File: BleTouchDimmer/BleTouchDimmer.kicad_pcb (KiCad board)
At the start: 2 copper layers, 28 parts, among them P1 PROG, P2 UART, Q1 PDTC123J, SW1 SW_PUSH, U1 LTV-814, U2 MDBT40, U3 MOC3021S, Y2 Crystal

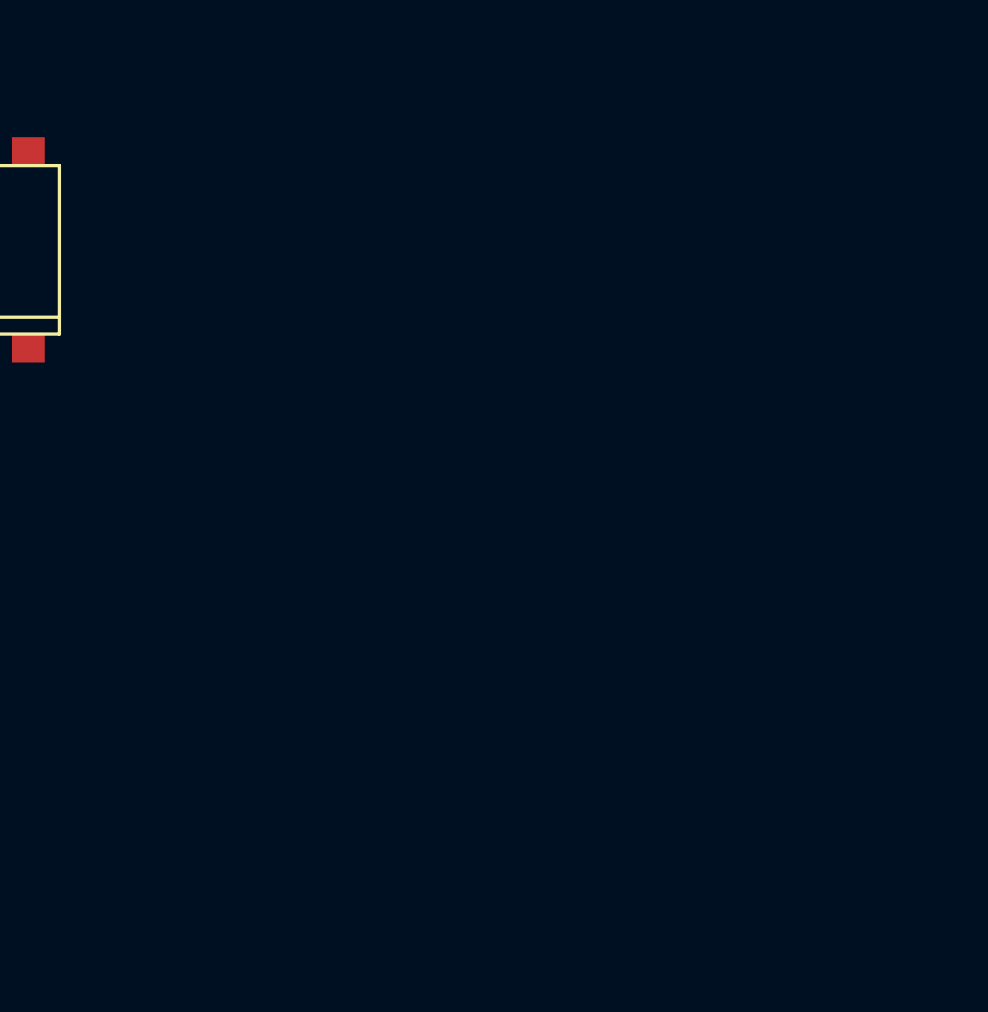
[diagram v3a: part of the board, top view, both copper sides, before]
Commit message: Added triacs.
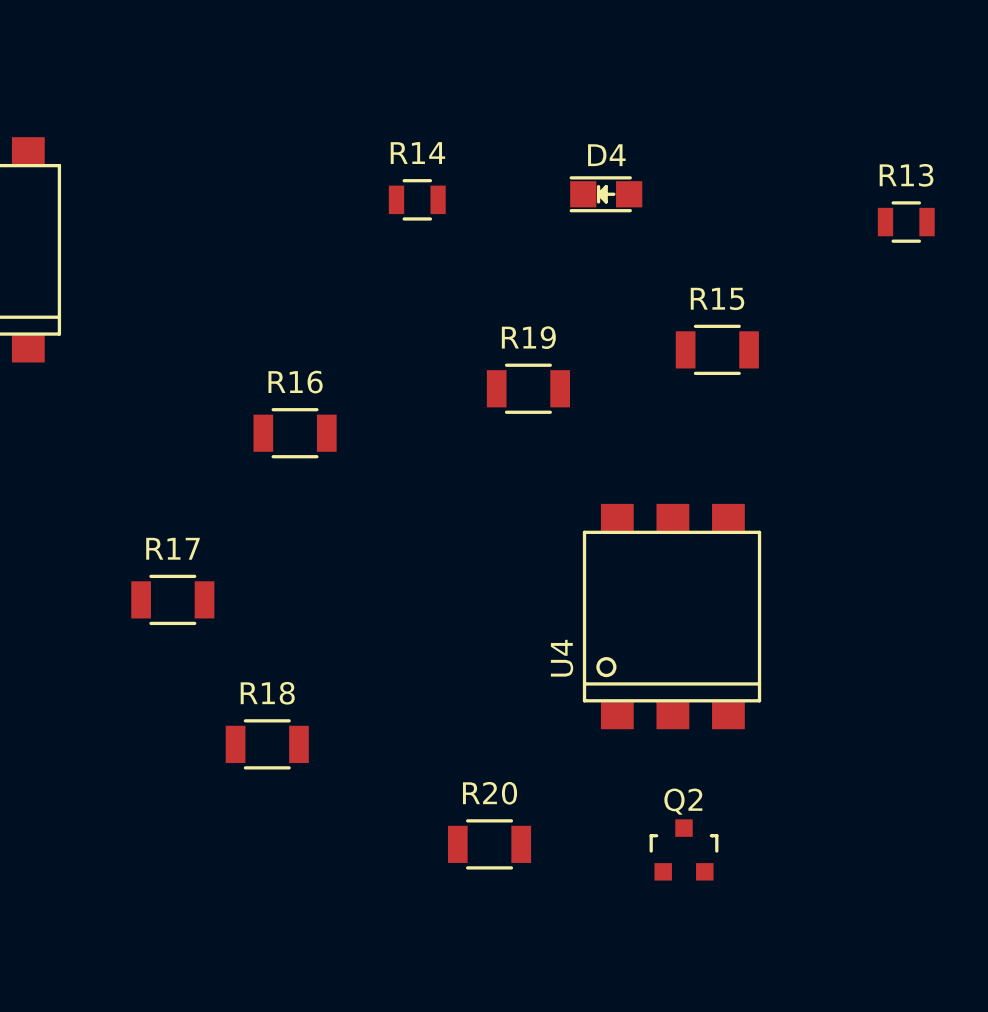
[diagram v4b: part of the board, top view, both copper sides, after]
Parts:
- added D4: LED, LEDs:LED_0805, F.Cu at (190.8, 68.6)
- added Q2: PDTC123J, TO_SOT_Packages_SMD:SOT-23, F.Cu at (194.3, 98.6)
- added R13: 100R, Resistors_SMD:R_0805, F.Cu at (204.5, 69.8)
- added R14: 220R, Resistors_SMD:R_0805, F.Cu at (182.1, 68.8)
- added R15: 360R, Resistors_SMD:R_1206, F.Cu at (195.8, 75.7)
- added R16: 360R, Resistors_SMD:R_1206, F.Cu at (176.5, 79.5)
- added R17: 360R, Resistors_SMD:R_1206, F.Cu at (170.9, 87.1)
- added R18: 360R, Resistors_SMD:R_1206, F.Cu at (175.3, 93.7)
- added R19: 360R, Resistors_SMD:R_1206, F.Cu at (187.2, 77.5)
- added R20: 360R, Resistors_SMD:R_1206, F.Cu at (185.4, 98.3)
- added U4: MOC3021S, EgertKiCad_lib:MOC3021S, F.Cu at (191.3, 87.9)
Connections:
- U3 pad 4: (no net) -> Net-(R16-Pad1)
- U3 pad 6: (no net) -> Net-(R15-Pad1)

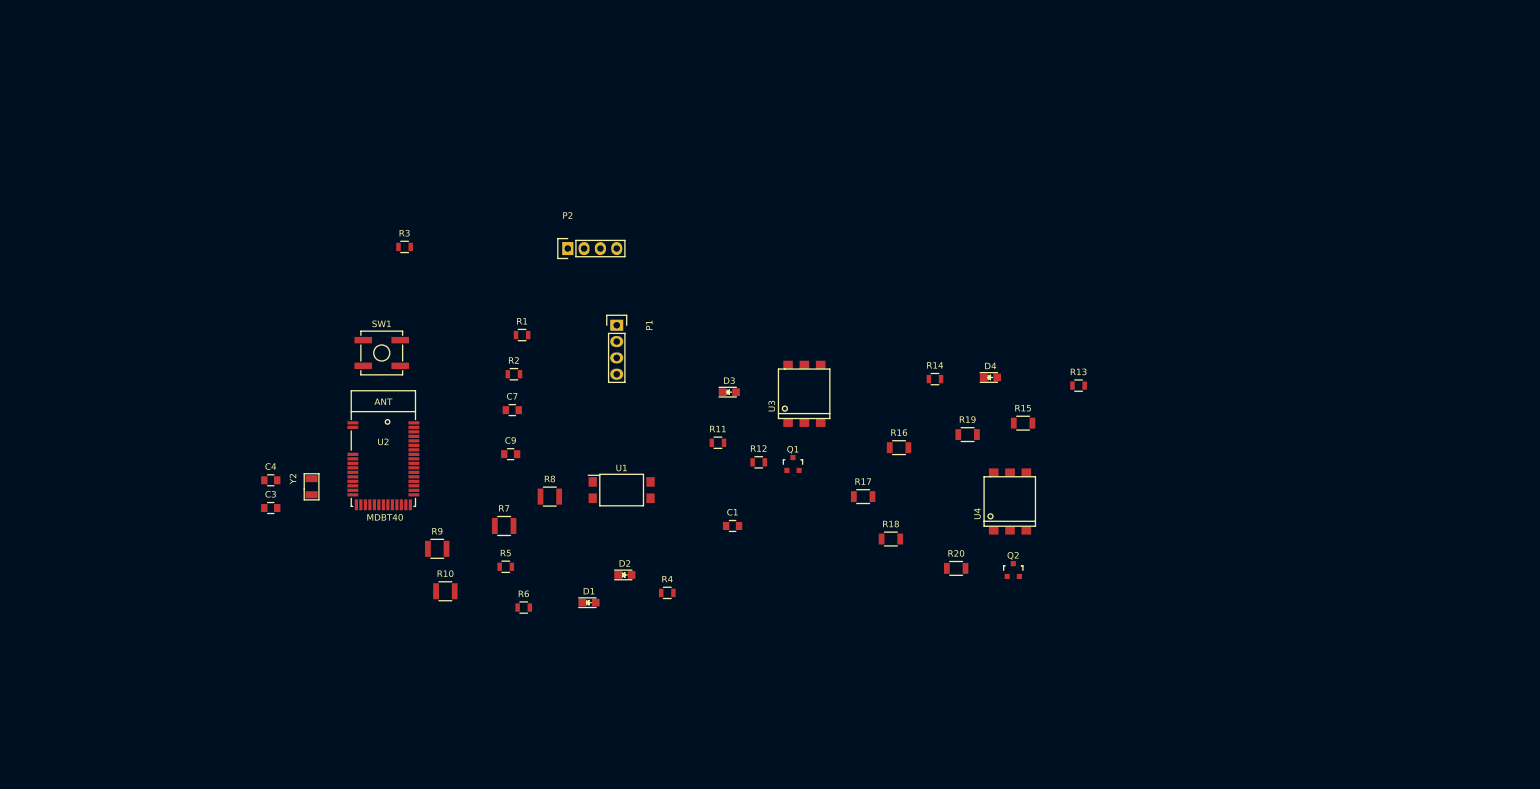
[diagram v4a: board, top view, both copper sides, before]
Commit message: Added isolation transformer:D
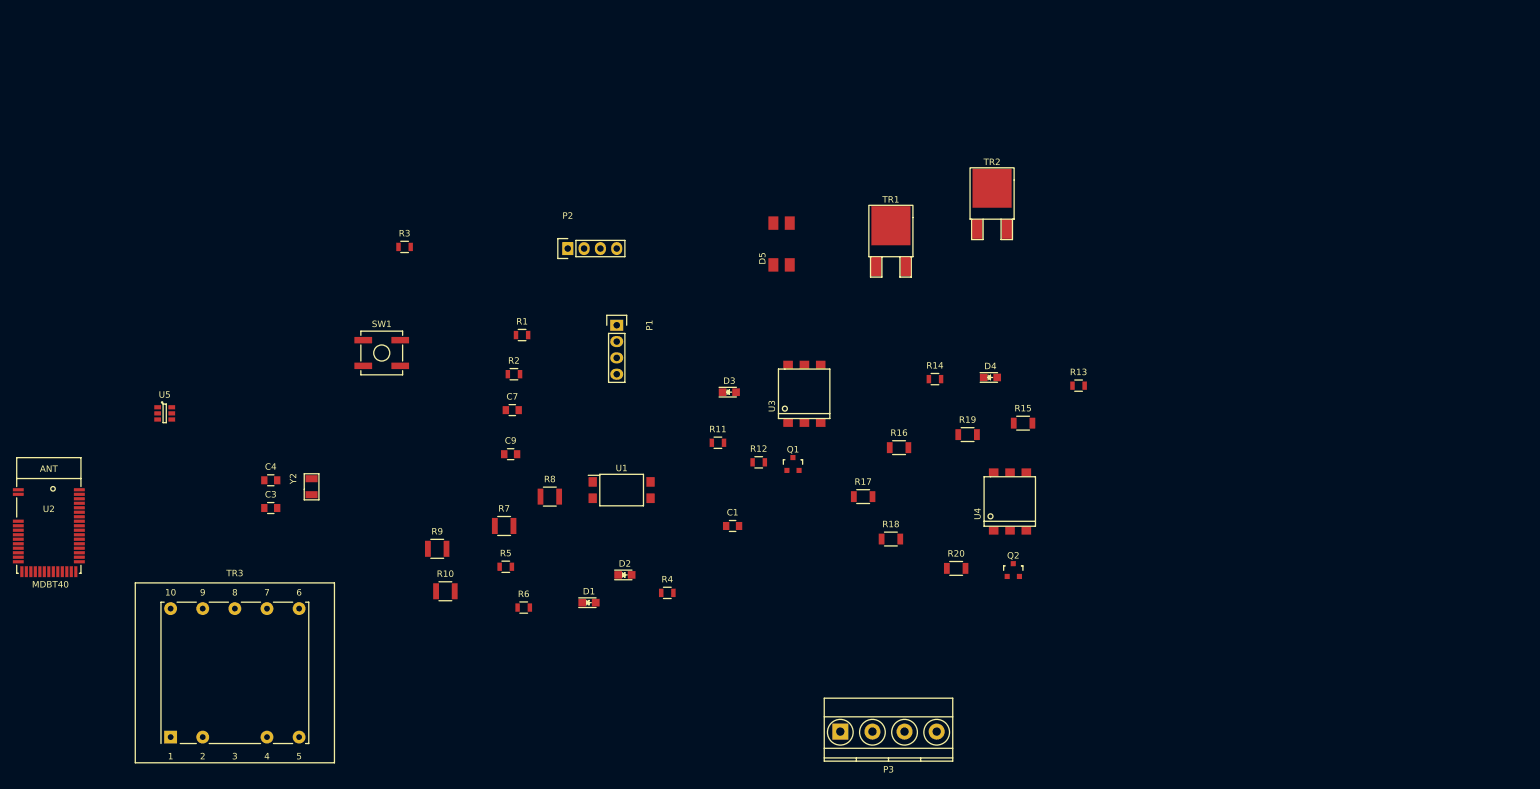
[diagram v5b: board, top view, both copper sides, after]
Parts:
- added D5: Diode_Bridge, EgertKiCad_lib:SOIC-4, F.Cu at (157.0, 51.1)
- added P3: POWER, Terminal_Blocks:TerminalBlock_Pheonix_MKDS1.5-4pol, F.Cu at (167.4, 123.7)
- added TR1: TRIAC, TO_SOT_Packages_SMD:TO-252-2Lead, F.Cu at (175.3, 51.3)
- added TR2: TRIAC, TO_SOT_Packages_SMD:TO-252-2Lead, F.Cu at (191.0, 45.5)
- added TR3: TEZ1.5-D-1, TEZ-28x33, F.Cu at (73.2, 114.6)
- added U5: LNK4002S, TO_SOT_Packages_SMD:SOT-23-6, F.Cu at (62.2, 74.2)
- moved U2 53.1 mm to (44.2, 99.1)
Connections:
- R19 pad 2: (no net) -> /TRIACS/TRIAC1_L_OUT
- R20 pad 2: (no net) -> /TRIACS/TRIAC2_L_OUT

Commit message: Updated schematic.
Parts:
- added C2: 100n, Capacitors_SMD:C_0603, F.Cu at (273.0, 36.6)
- added C6: 10uF, Capacitors_SMD:C_0603, F.Cu at (226.9, 68.4)
- added C8: 22uF, Capacitors_SMD:C_0603, F.Cu at (218.8, 73.0)
- added D6: Led_Small, LEDs:LED_0603, F.Cu at (220.7, 68.1)
- added J1: Conn_01x03, Connectors_Molex:Molex_SPOX-5267_22-03-5035_03x2.54mm_Straight, F.Cu at (237.5, 47.3)
- added J2: Conn_01x03, Connectors_Molex:Molex_SPOX-5267_22-03-5035_03x2.54mm_Straight, F.Cu at (255.5, 38.9)
- added J3: JTAG, Connectors_Molex:Molex_SPOX-5267_22-03-5075_07x2.54mm_Straight, F.Cu at (219.4, 38.9)
- added J4: Conn_01x06, Connectors_Molex:Molex_SPOX-5267_22-03-5065_06x2.54mm_Straight, F.Cu at (219.4, 47.3)
- added J5: SLIDER1, Connectors_Molex:Molex_SPOX-5267_22-03-5055_05x2.54mm_Straight, F.Cu at (240.0, 38.9)
- added J6: SLIDER2, Connectors_Molex:Molex_SPOX-5267_22-03-5055_05x2.54mm_Straight, F.Cu at (219.4, 55.7)
- added Q3: PDTC123J, TO_SOT_Packages_SMD:SOT-23, F.Cu at (249.2, 46.0)
- added Q4: PDTC123J, TO_SOT_Packages_SMD:SOT-23, F.Cu at (249.2, 53.0)
- added Q5: BC850, TO_SOT_Packages_SMD:SOT-23, F.Cu at (261.2, 46.0)
- added Q6: BC850, TO_SOT_Packages_SMD:SOT-23, F.Cu at (255.8, 46.0)
- added R21: 100R, Resistors_SMD:R_0603, F.Cu at (223.1, 73.4)
- added R23: 0R, Resistors_SMD:R_0603, F.Cu at (243.9, 59.0)
- added R24: 0R, Resistors_SMD:R_0603, F.Cu at (265.0, 36.5)
- added R25: 0R, Resistors_SMD:R_0603, F.Cu at (254.9, 52.0)
- added R26: 0R, Resistors_SMD:R_0603, F.Cu at (247.3, 59.0)
- added R27: 2k2, Resistors_SMD:R_0603, F.Cu at (258.3, 52.0)
- added R28: 2k2, Resistors_SMD:R_0603, F.Cu at (250.8, 59.0)
- added R29: 10k, Resistors_SMD:R_0603, F.Cu at (254.9, 57.0)
- added VR1: VR, Varistors:RV_Disc_D9_W4.4_P5, F.Cu at (234.7, 54.1)
- C1: value 1n -> 10u; footprint Capacitors_SMD:C_0805 -> Capacitors_SMD:C_0603
- C3: value 22pF -> 1n; footprint Capacitors_SMD:C_0805 -> Capacitors_SMD:C_0603
- C7: value 1u -> 100n; footprint Capacitors_SMD:C_0805 -> Capacitors_SMD:C_0603
- D1, D2, D3, D4: footprint LEDs:LED_0805 -> LEDs:LED_0603
- R1, R2: value 10k -> 100R; footprint Resistors_SMD:R_0805 -> Resistors_SMD:R_0603
- R11, R12, R13, R14, R3, R4, R5, R6: footprint Resistors_SMD:R_0805 -> Resistors_SMD:R_0603
- U5: value LNK4002S -> LD1117S33TR; footprint TO_SOT_Packages_SMD:SOT-23-6 -> SOT-223
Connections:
- C1 pad 1: GND -> +3V3
- C1 pad 2: /Reset/SWDIO/RESET -> GND
- C3 pad 2: Net-(C3-Pad2) -> /RESET
- D2 pad 1: /ZC_DETECT/ZC_DETECT -> /ZC_DETECT
- D5 pad 1: (no net) -> GND
- D5 pad 2: (no net) -> GND
- D5 pad 3: (no net) -> Net-(C5-Pad1)
- D5 pad 4: (no net) -> Net-(D5-Pad4)
- P3 pad 1: (no net) -> /L_IN
- P3 pad 2: (no net) -> /TR1_L_OUT
- P3 pad 3: (no net) -> /TR2_L_OUT
- P3 pad 4: (no net) -> /N
- Q1 pad 1: (no net) -> /TR1_CTRL
- Q2 pad 1: (no net) -> /TR2_CTRL
- R1 pad 1: GND -> +3V3
- R1 pad 2: /SWDCLK -> Net-(J1-Pad3)
- R10 pad 1: (no net) -> /N
- R15 pad 2: /TRIACS/230VAC_L -> /230_VAC_L
- R17 pad 2: /TRIACS/230VAC_L -> /230_VAC_L
- R19 pad 2: /TRIACS/TRIAC1_L_OUT -> /TR1_L_OUT
- R2 pad 1: /Reset/SWDIO/RESET -> +3V3
- R2 pad 2: +3V3 -> Net-(J2-Pad3)
- R20 pad 2: /TRIACS/TRIAC2_L_OUT -> /TR2_L_OUT
- R4 pad 2: Net-(R4-Pad2) -> /DEBUG_LED
- R6 pad 2: /ZC_DETECT/ZC_DETECT -> /ZC_DETECT
- R9 pad 1: (no net) -> /230_VAC_L
- SW1 pad 1: /Reset/SWDIO/RESET -> /RESET
- TR1 pad 1: /TRIACS/TRIAC1_L_OUT -> /TR1_L_OUT
- TR1 pad 2: /TRIACS/230VAC_L -> /230_VAC_L
- TR2 pad 1: /TRIACS/TRIAC2_L_OUT -> /TR2_L_OUT
- TR2 pad 2: /TRIACS/230VAC_L -> /230_VAC_L
- TR3 pad 1: (no net) -> /230_VAC_L
- TR3 pad 5: (no net) -> /N
- TR3 pad 7: (no net) -> Net-(D5-Pad4)
- TR3 pad 9: (no net) -> GND
- U1 pad 4: /ZC_DETECT/ZC_DETECT -> /ZC_DETECT
- U3 pad 3: (no net) -> Net-(U3-Pad3)
- U3 pad 5: (no net) -> Net-(U3-Pad5)
- U4 pad 3: (no net) -> Net-(U4-Pad3)
- U4 pad 5: (no net) -> Net-(U4-Pad5)
- U5 pad 1: (no net) -> GND
- U5 pad 2: (no net) -> +3V3
- U5 pad 3: (no net) -> Net-(C5-Pad1)

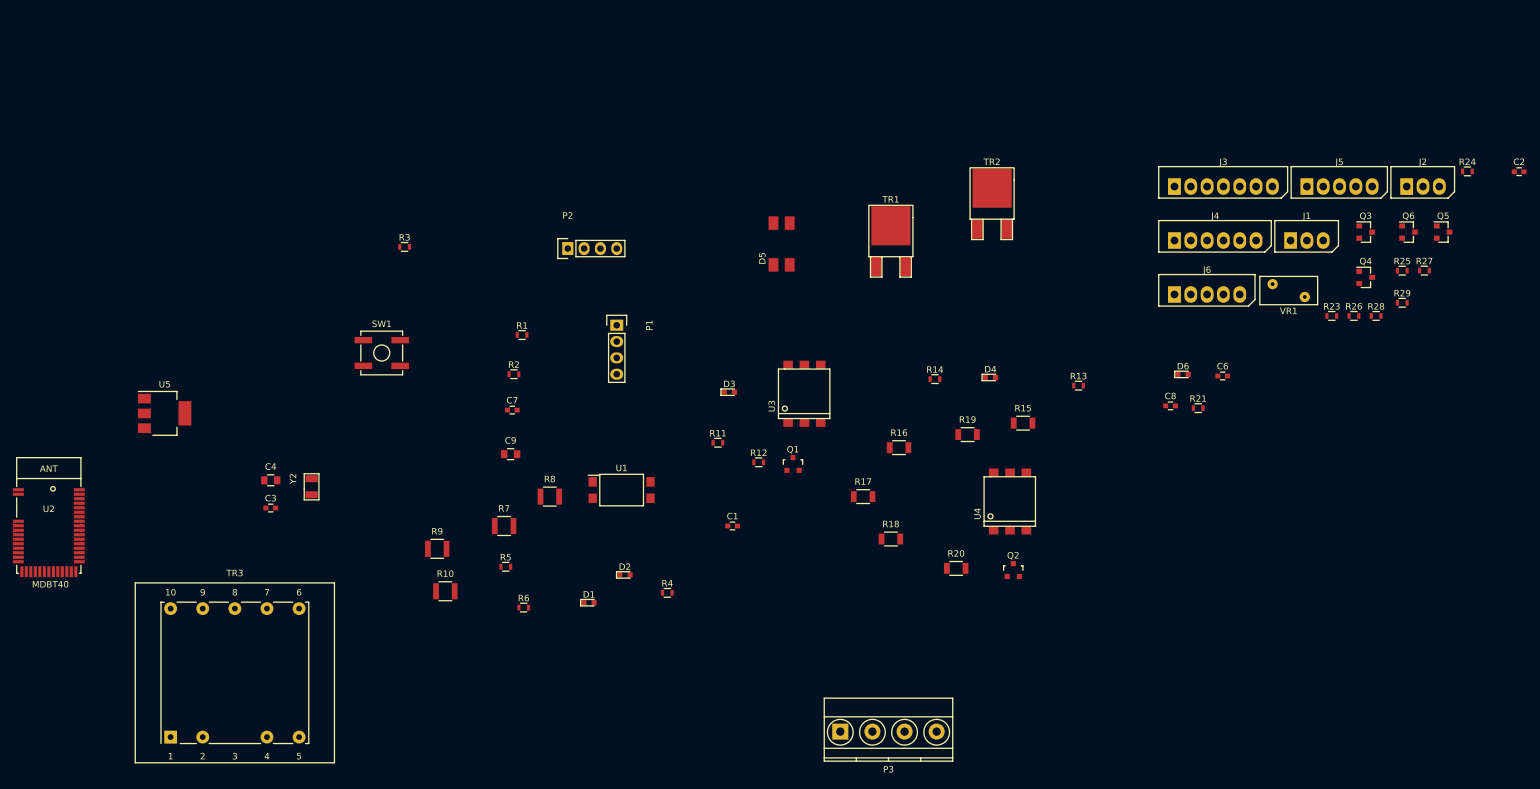
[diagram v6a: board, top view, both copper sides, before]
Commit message: Started placing footprints on pcb. Maybe needs to split pcb to power part and controller part.
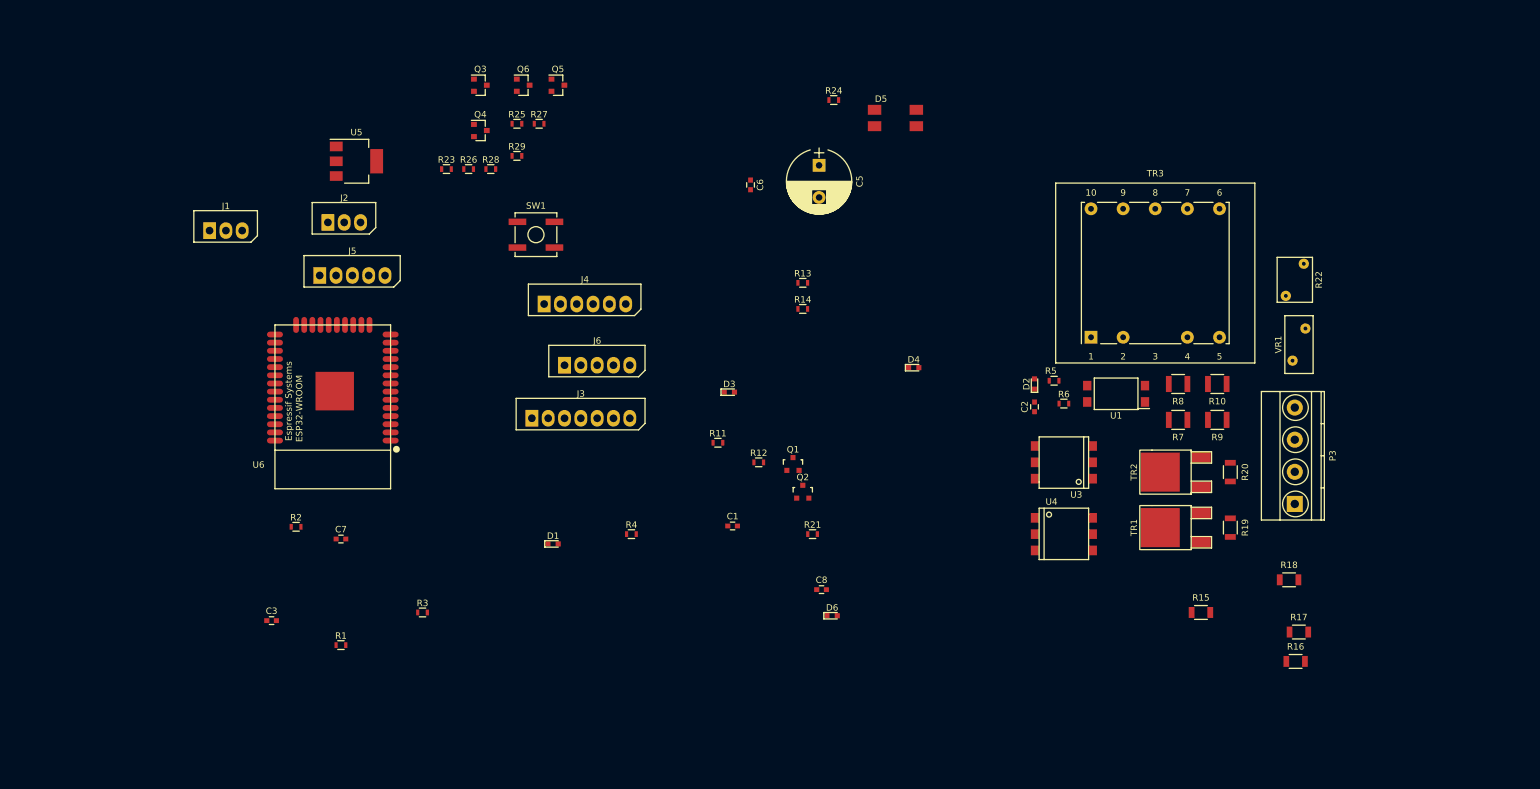
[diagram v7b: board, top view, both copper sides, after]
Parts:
- removed C4: 22pF, Capacitors_SMD:C_0805
- removed C9: 1u, Capacitors_SMD:C_0805
- removed P1: PROG, Socket_Strips:Socket_Strip_Straight_1x04
- removed P2: UART, Socket_Strips:Socket_Strip_Straight_1x04
- removed U2: MDBT40, EgertKiCad_lib:MDBT40
- removed Y2: Crystal, EgertKiCad_lib:Crystal_ECX-31B
- added C5: 1000uF, Capacitors_ThroughHole:CP_Radial_D10.0mm_P5.00mm, F.Cu at (164.1, 35.6)
- added R22: PTCC, Varistors:RV_Disc_D7_W5.5_P5, F.Cu at (236.7, 55.9)
- added U6: ESP32-WROOM, esp_library:ESP32-WROOM, F.Cu at (88.4, 73.2)
- D5: value Diode_Bridge -> D_Bridge_+-AA
- moved J1 168.3 mm to (69.2, 45.7)
- moved J2 168.0 mm to (87.6, 44.5)
- moved TR3 156.2 mm to (216.4, 52.3)
- moved J5 154.3 mm to (86.4, 52.7)
- moved Q3 139.7 mm to (111.4, 23.1)
- moved Q4 139.7 mm to (111.4, 30.1)
- moved Q5 139.7 mm to (123.4, 23.1)
- moved Q6 139.7 mm to (118.0, 23.1)
- moved R23 139.7 mm to (106.1, 36.1)
- moved R25 139.7 mm to (117.1, 29.1)
- moved R28 139.7 mm to (113.0, 36.1)
- moved R29 139.7 mm to (117.1, 34.1)
- moved R26 139.7 mm to (109.5, 36.1)
- moved R27 139.7 mm to (120.5, 29.1)
- moved R10 124.4 mm to (226.1, 69.6), turned to 180 degrees
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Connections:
- D5 pad 1: GND -> Net-(C5-Pad1)
- D5 pad 3: Net-(C5-Pad1) -> Net-(D5-Pad3)
- TR3 pad 9: GND -> Net-(D5-Pad3)
- U3 pad 3: Net-(U3-Pad3) -> (no net)
- U3 pad 5: Net-(U3-Pad5) -> (no net)
- U4 pad 3: Net-(U4-Pad3) -> (no net)
- U4 pad 5: Net-(U4-Pad5) -> (no net)
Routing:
- net /N: track 0.00 -> 0.89 mm
